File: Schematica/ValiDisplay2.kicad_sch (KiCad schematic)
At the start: 14 parts, among them Q1 2N3904, Q2 2N3904, Q3 2N3904, Q4 2N3904, SW1 Reset, U1 CA56-12EWA

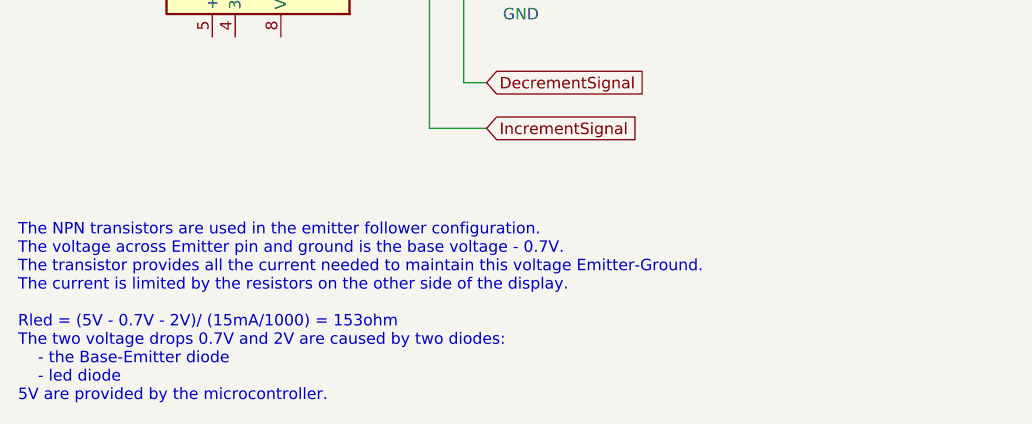
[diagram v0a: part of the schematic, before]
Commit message: Added showDisplay function
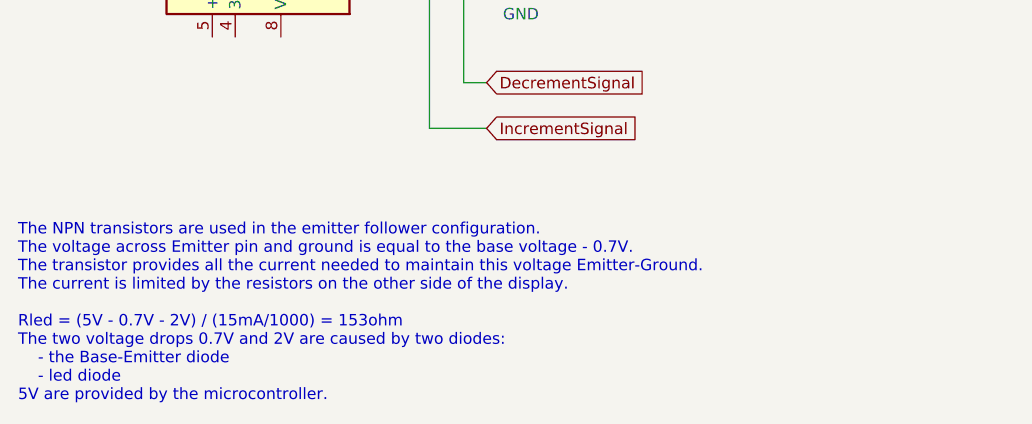
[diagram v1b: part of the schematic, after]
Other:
- note added: "The NPN transistors are used in the emitter follower configuration. The voltage across Emitter pin and ground is equal to the base voltage - 0.7V. The transistor provides all the current needed to maintain this voltage Emitter-Ground. The current is limited by the resistors on the other side of the display. Rled = (5V - 0.7V - 2V) / (15mA/1000) = 153ohm The two voltage drops 0.7V and 2V are cause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"
- note removed: "The NPN transistors are used in the emitter follower configuration. The voltage across Emitter pin and ground is the base voltage - 0.7V. The transistor provides all the current needed to maintain this voltage Emitter-Ground. The current is limited by the resistors on the other side of the display. Rled = (5V - 0.7V - 2V)/ (15mA/1000) = 153ohm The two voltage drops 0.7V and 2V are caused by two d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"
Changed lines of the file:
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@@
     (stroke (width 0) (type default) (color 0 0 0 0))
   )
-  (text "The NPN transistors are used in the emitter follower configuration.\nThe voltage across Emitter pin and ground is the base voltage - 0.7V.\nThe transistor provides all the current needed to maintain this voltage Emitter-Ground.\nThe current is limited by the resistors on the other side of the display.\n\nRled = (5V - 0.7V - 2V)/ (15mA/1000) = 153ohm\nThe two voltage drops 0.7V and 2V are caused by two diodes:\n	- the Base-Emitter diode\n	- led diode\n5V are provided by the microcontroller."
+  (text "The NPN transistors are used in the emitter follower configuration.\nThe voltage across Emitter pin and ground is equal to the base voltage - 0.7V.\nThe transistor provides all the current needed to maintain this voltage Emitter-Ground.\nThe current is limited by the resistors on the other side of the display.\n\nRled = (5V - 0.7V - 2V) / (15mA/1000) = 153ohm\nThe two voltage drops 0.7V and 2V are caused by two diodes:\n	- the Base-Emitter diode\n	- led diode\n5V are provided by the microcontroller."
     (at 45.72 175.26 0)
     (effects (font (size 1.27 1.27)) (justify left bottom))
